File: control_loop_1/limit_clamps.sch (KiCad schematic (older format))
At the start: 56 parts, among them Q1 2N7002BK, Q2 2N7002BK, Q3 2N7002BK, Q4 2N7002BK, U7 OPA1679IDR, U8 LM393BIDR, U9 LM393BIDR

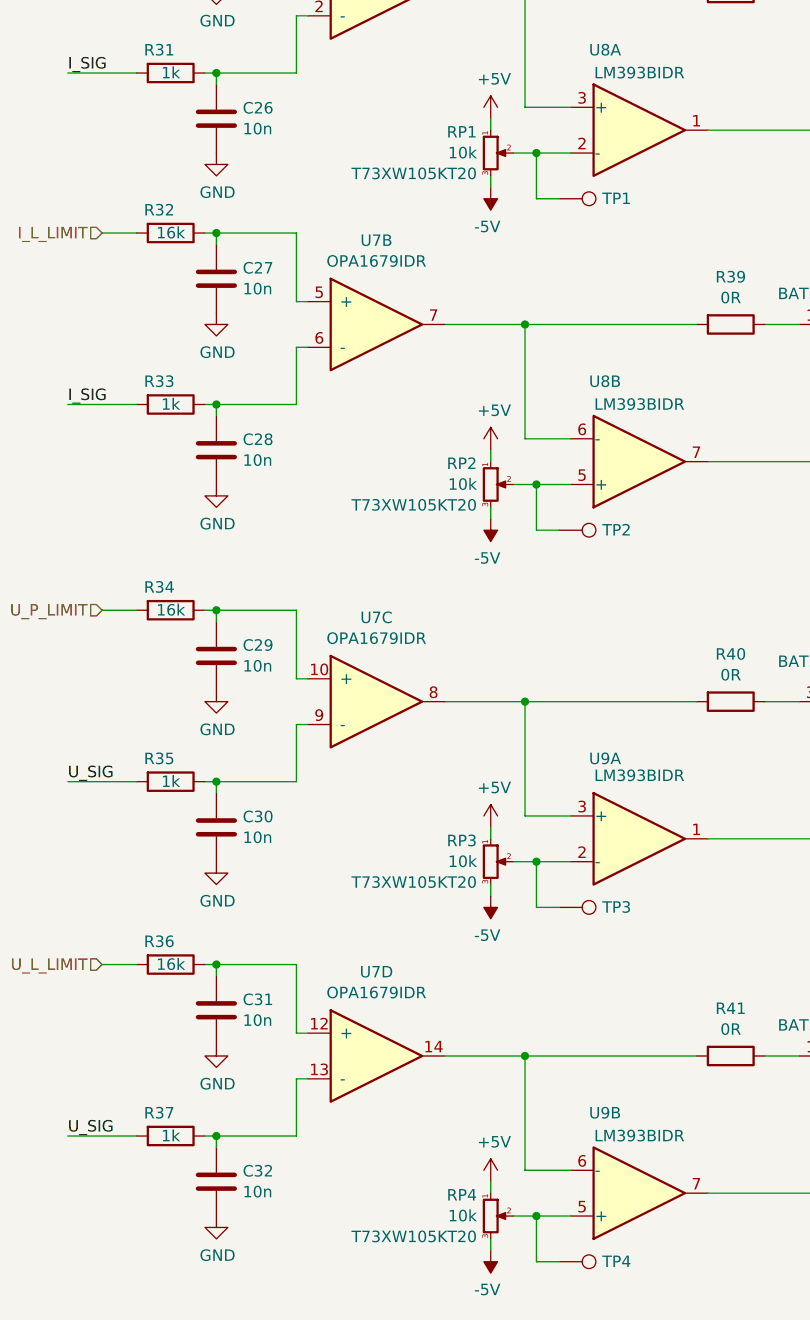
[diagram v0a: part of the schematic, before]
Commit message: fixed diodes orientation
negative volt regulator - reversed diodes fixed
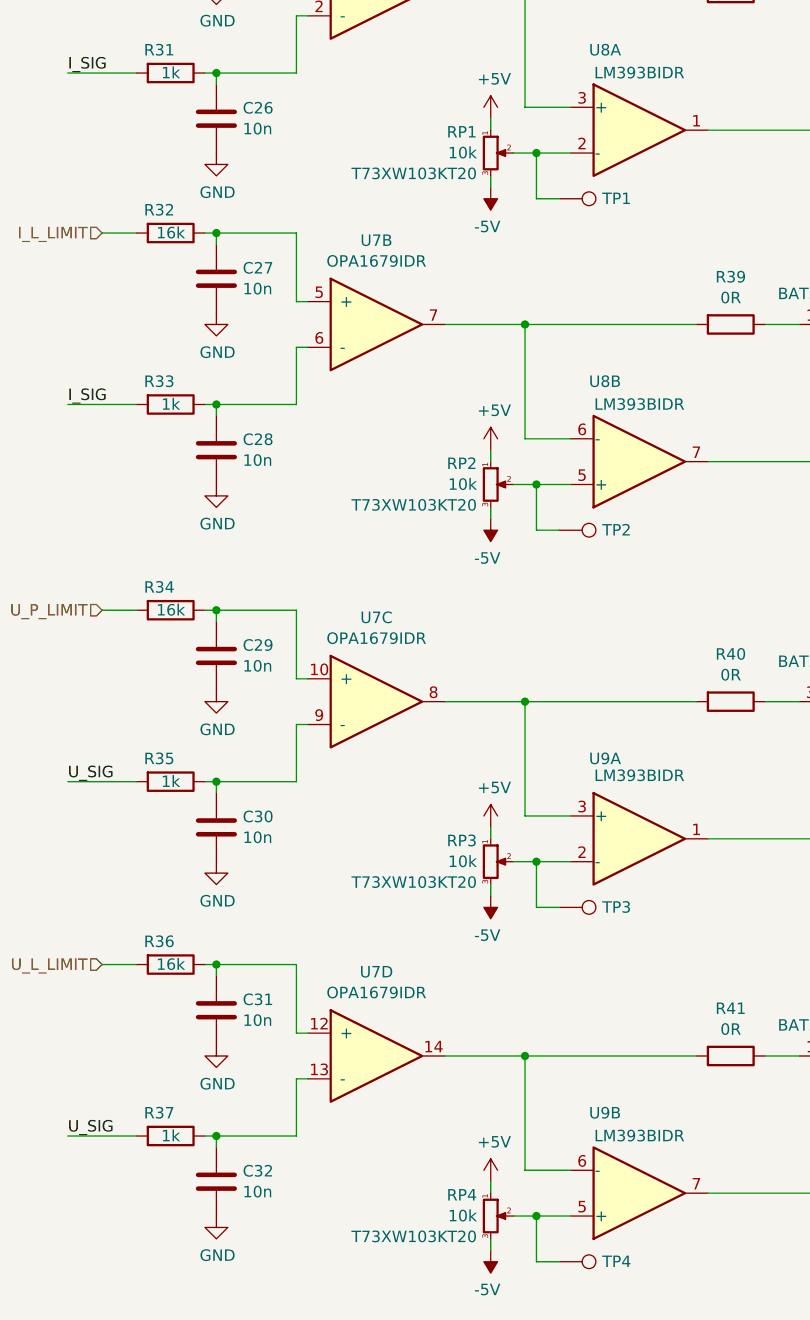
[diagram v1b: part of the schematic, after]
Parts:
- RP1, RP2, RP3, RP4: MPN T73XW105KT20 -> T73XW103KT20
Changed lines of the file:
@@
 F 2 "Potentiometer_THT:Potentiometer_Vishay_T73XW_Horizontal" H 2900 6900 50  0001 C CNN
 F 3 "https://pl.mouser.com/datasheet/2/427/t73-1764337.pdf" H 2900 6900 50  0001 C CNN
-F 4 "T73XW105KT20" H 2840 6809 50  0000 R CNN "MPN"
+F 4 "T73XW103KT20" H 2840 6809 50  0000 R CNN "MPN"
 	1    2900 6900
 	1    0    0    -1
@@
 F 2 "Potentiometer_THT:Potentiometer_Vishay_T73XW_Horizontal" H 2900 5350 50  0001 C CNN
 F 3 "https://pl.mouser.com/datasheet/2/427/t73-1764337.pdf" H 2900 5350 50  0001 C CNN
-F 4 "T73XW105KT20" H 2840 5259 50  0000 R CNN "MPN"
+F 4 "T73XW103KT20" H 2840 5259 50  0000 R CNN "MPN"
 	1    2900 5350
 	1    0    0    -1
@@
 F 2 "Potentiometer_THT:Potentiometer_Vishay_T73XW_Horizontal" H 2900 3700 50  0001 C CNN
 F 3 "https://pl.mouser.com/datasheet/2/427/t73-1764337.pdf" H 2900 3700 50  0001 C CNN
-F 4 "T73XW105KT20" H 2840 3609 50  0000 R CNN "MPN"
+F 4 "T73XW103KT20" H 2840 3609 50  0000 R CNN "MPN"
 	1    2900 3700
 	1    0    0    -1
@@
 F 2 "Potentiometer_THT:Potentiometer_Vishay_T73XW_Horizontal" H 2900 2250 50  0001 C CNN
 F 3 "https://pl.mouser.com/datasheet/2/427/t73-1764337.pdf" H 2900 2250 50  0001 C CNN
-F 4 "T73XW105KT20" H 2840 2159 50  0000 R CNN "MPN"
+F 4 "T73XW103KT20" H 2840 2159 50  0000 R CNN "MPN"
 	1    2900 2250
 	1    0    0    -1
